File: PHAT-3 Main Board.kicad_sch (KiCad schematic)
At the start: 2 parts, among them U1 BY-68 BMP180, U2 ESP32-S3 Dual-core SX1262

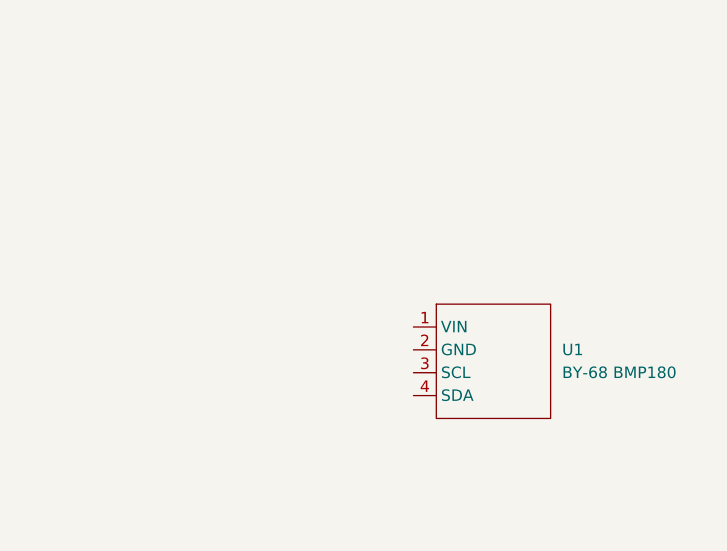
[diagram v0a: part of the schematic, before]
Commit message: Added AHT21 I2C IIC
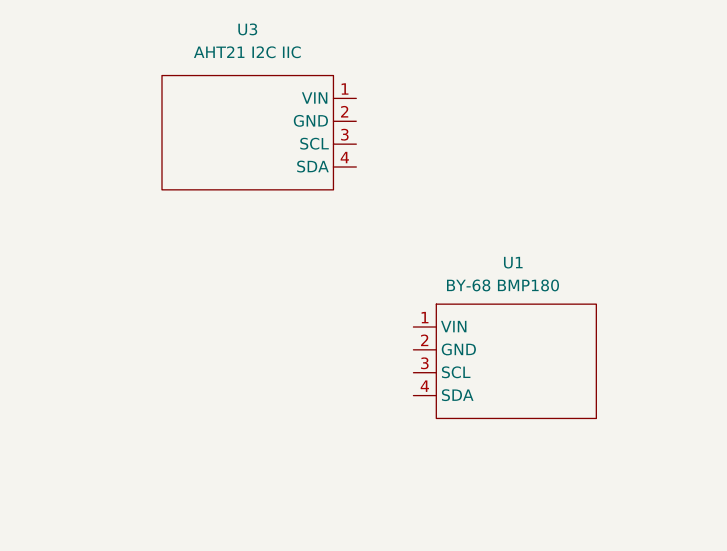
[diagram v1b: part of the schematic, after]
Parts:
- added U3: AHT21 I2C IIC, Actual Footprint Library:AHT21 I2C IIC, symbol Footprint Library:AHT21_I2C_IIC
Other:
- moved on the sheet: U1
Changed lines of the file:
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@@
 	(paper "A4")
+	(symbol
+		(lib_id "Footprint Library:AHT21_I2C_IIC")
+		(at 151.13 66.04 0)
+		(unit 1)
+		(exclude_from_sim no)
+		(in_bom yes)
+		(on_board yes)
+		(dnp no)
+		(fields_autoplaced yes)
+		(property "Reference" "U3"
+			(at 139.065 50.8 0)
+			(effects
+				(font
+					(size 1.27 1.27)
+				)
+			)
+		)
+		(property "Value" "AHT21 I2C IIC"
+			(at 139.065 53.34 0)
+			(effects
+				(font
+					(size 1.27 1.27)
+				)
+			)
+		)
+		(property "Footprint" "Actual Footprint Library:AHT21 I2C IIC"
+			(at 150.368 74.168 0)
+			(effects
+				(font
+					(size 1.27 1.27)
+				)
+				(hide yes)
+			)
+		)
+		(property "Datasheet" ""
+			(at 151.13 66.04 0)
+			(effects
+				(font
+					(size 1.27 1.27)
+				)
+				(hide yes)
+			)
+		)
+		(property "Description" ""
+			(at 151.13 66.04 0)
+			(effects
+				(font
+					(size 1.27 1.27)
+				)
+				(hide yes)
+			)
+		)
+		(pin "1"
+		)
+		(pin "2"
+		)
+		(pin "3"
+		)
+		(pin "4"
+		)
+		(instances
+			(project ""
+				(path "/da389c8a-9ca2-41c4-a7eb-3ce46ba4333b"
+					(reference "U3")
+					(unit 1)
+				)
+			)
+		)
+	)
 	(symbol
 		(lib_id "Footprint Library:ESP32-S3_Dual-core_SX1262")
@@
 		(on_board yes)
 		(dnp no)
-		(fields_autoplaced yes)
 		(property "Reference" "U1"
-			(at 173.99 86.3599 0)
+			(at 167.386 76.708 0)
 			(effects
 				(font
@@
 		)
 		(property "Value" "BY-68 BMP180"
-			(at 173.99 88.8999 0)
-			(effects
-				(font
+			(at 161.036 79.248 0)
+			(effects
+				(font

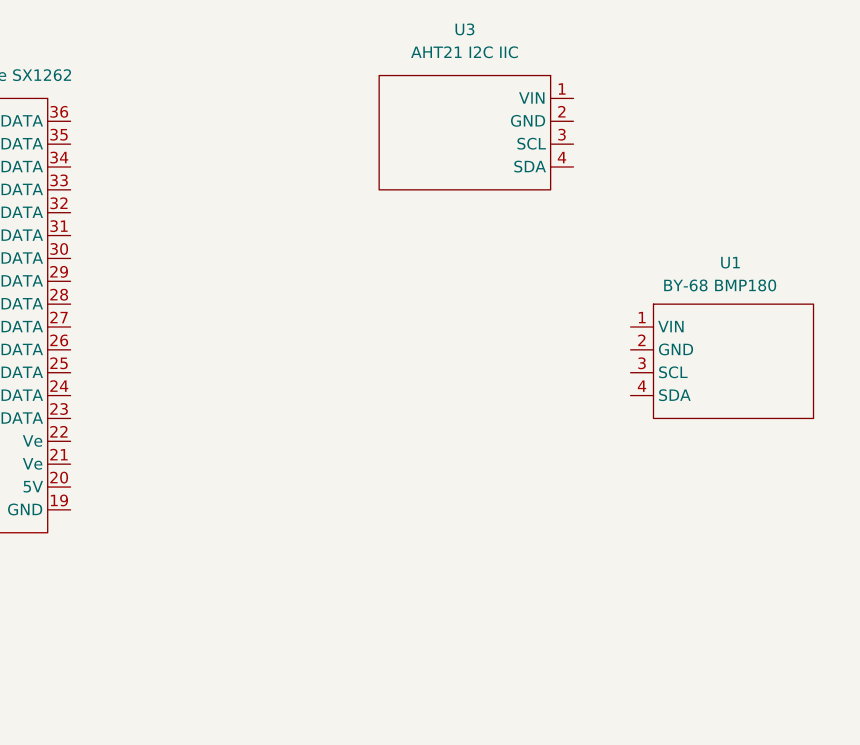
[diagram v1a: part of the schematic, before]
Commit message: Added Buck Converter and Rest of Sensors
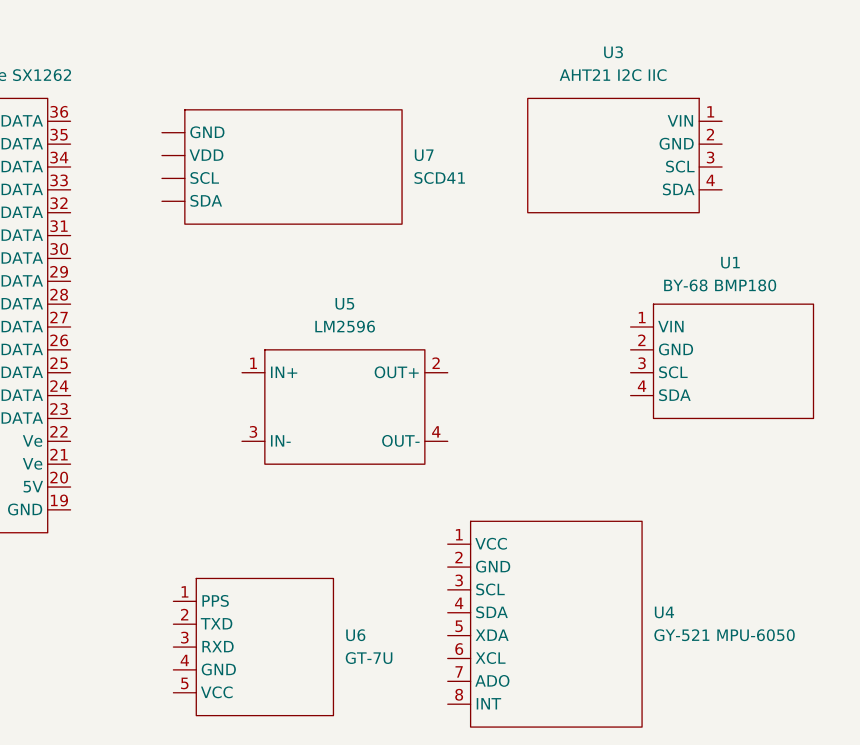
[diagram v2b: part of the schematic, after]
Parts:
- added U4: GY-521 MPU-6050, Actual Footprint Library:GY-521 MPU-6050, symbol Footprint Library:GY-521_MPU-6050
- added U5: LM2596, Actual Footprint Library:LM2596, symbol Footprint Library:LM2596
- added U6: GT-7U, Actual Footprint Library:GT-U7, symbol Footprint Library:GT-7U
- added U7: SCD41, Actual Footprint Library:SCD41, symbol Footprint Library:SCD41
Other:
- moved on the sheet: U3

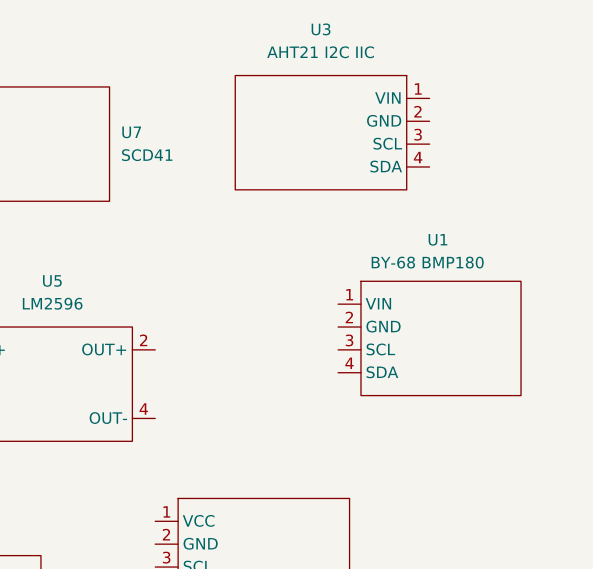
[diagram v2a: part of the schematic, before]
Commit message: Updated GY-BMP180 to BME280
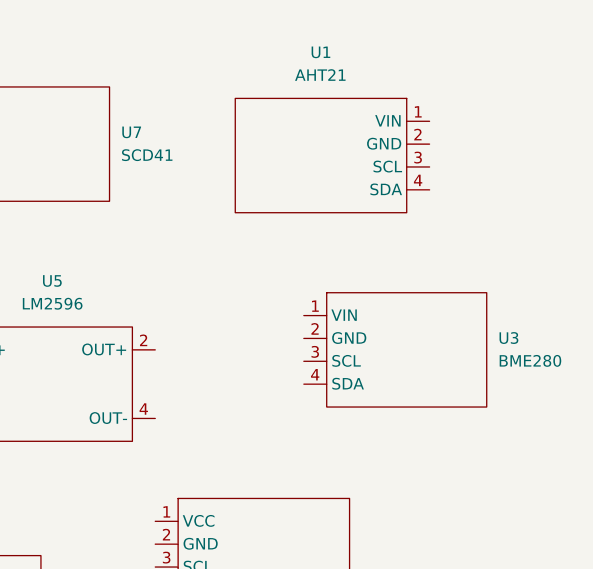
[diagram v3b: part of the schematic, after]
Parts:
- removed U1: BY-68 BMP180, Actual Footprint Library:BY-68 BMP180, symbol Footprint Library:GY-68_BMP180
- removed U3: AHT21 I2C IIC, Actual Footprint Library:AHT21 I2C IIC, symbol Footprint Library:AHT21_I2C_IIC
- added U1: AHT21, Actual Footprint Library:AHT21, symbol Footprint Library:AHT21
- added U3: BME280, Actual Footprint Library:BME280, symbol Footprint Library:BME280
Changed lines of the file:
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@@
-	)
-	(symbol
-		(lib_id "Footprint Library:AHT21_I2C_IIC")
-		(at 167.64 68.58 0)
-		(unit 1)
-		(exclude_from_sim no)
-		(in_bom yes)
-		(on_board yes)
-		(dnp no)
-		(fields_autoplaced yes)
-		(property "Reference" "U3"
-			(at 155.575 53.34 0)
-			(effects
-				(font
-					(size 1.27 1.27)
-				)
-			)
-		)
-		(property "Value" "AHT21 I2C IIC"
-			(at 155.575 55.88 0)
-			(effects
-				(font
-					(size 1.27 1.27)
-				)
-			)
-		)
-		(property "Footprint" "Actual Footprint Library:AHT21 I2C IIC"
-			(at 166.878 76.708 0)
-			(effects
-				(font
-					(size 1.27 1.27)
-				)
-				(hide yes)
-			)
-		)
-		(property "Datasheet" ""
-			(at 167.64 68.58 0)
-			(effects
-				(font
-					(size 1.27 1.27)
-				)
-				(hide yes)
-			)
-		)
-		(property "Description" ""
-			(at 167.64 68.58 0)
-			(effects
-				(font
-					(size 1.27 1.27)
-				)
-				(hide yes)
-			)
-		)
-		(pin "1"
-		)
-		(pin "2"
-		)
-		(pin "3"
-		)
-		(pin "4"
-		)
-		(instances
-			(project ""
-				(path "/da389c8a-9ca2-41c4-a7eb-3ce46ba4333b"
-					(reference "U3")
-					(unit 1)
-				)
-			)
-		)
 	)
 	(symbol
@@
 	)
 	(symbol
+		(lib_id "Footprint Library:AHT21")
+		(at 167.64 71.12 0)
+		(unit 1)
+		(exclude_from_sim no)
+		(in_bom yes)
+		(on_board yes)
+		(dnp no)
+		(fields_autoplaced yes)
+		(property "Reference" "U1"
+			(at 155.575 55.88 0)
+			(effects
+				(font
+					(size 1.27 1.27)
+				)
+			)
+		)
+		(property "Value" "AHT21"
+			(at 155.575 58.42 0)
+			(effects
+				(font
+					(size 1.27 1.27)
+				)
+			)
+		)
+		(property "Footprint" "Actual Footprint Library:AHT21"
+			(at 166.878 79.248 0)
+			(effects
+				(font
+					(size 1.27 1.27)
+				)
+				(hide yes)
+			)
+		)
+		(property "Datasheet" ""
+			(at 167.64 71.12 0)
+			(effects
+				(font
+					(size 1.27 1.27)
+				)
+				(hide yes)
+			)
+		)
+		(property "Description" ""
+			(at 167.64 71.12 0)
+			(effects
+				(font
+					(size 1.27 1.27)
+				)
+				(hide yes)
+			)
+		)
+		(pin "4"
+		)
+		(pin "2"
+		)
+		(pin "1"
+		)
+		(pin "3"
+		)
+		(instances
+			(project ""
+				(path "/da389c8a-9ca2-41c4-a7eb-3ce46ba4333b"
+					(reference "U1")
+					(unit 1)
+				)
+			)
+		)
+	)
+	(symbol
 		(lib_id "Footprint Library:ESP32-S3_Dual-core_SX1262")
 		(at 71.12 104.14 0)
@@
 	)
 	(symbol
-		(lib_id "Footprint Library:GY-68_BMP180")
-		(at 157.48 91.44 0)
+		(lib_id "Footprint Library:BME280")
+		(at 153.67 92.71 0)
 		(unit 1)
 		(exclude_from_sim no)
@@
 		(on_board yes)
 		(dnp no)
-		(property "Reference" "U1"
-			(at 167.386 76.708 0)
+		(fields_autoplaced yes)
+		(property "Reference" "U3"
+			(at 175.26 87.6299 0)
 			(effects
 				(font
@@
 			)
 		)
-		(property "Value" "BY-68 BMP180"
-			(at 161.036 79.248 0)
+		(property "Value" "BME280"
+			(at 175.26 90.1699 0)
 			(effects
 				(font
@@
 			)
 		)
-		(property "Footprint" "Actual Footprint Library:BY-68 BMP180"
-			(at 159.004 100.076 0)
+		(property "Footprint" "Actual Footprint Library:BME280"
+			(at 155.194 101.346 0)
 			(effects
 				(font
@@
 		)
 		(property "Datasheet" ""
-			(at 157.48 91.44 0)
+			(at 153.67 92.71 0)
 			(effects
 				(font
@@
 		)
 		(property "Description" ""
-			(at 157.48 91.44 0)
-			(effects
-				(font
-					(size 1.27 1.27)
-				)
-				(hide yes)
-			)
+			(at 153.67 92.71 0)
+			(effects
+				(font
+					(size 1.27 1.27)
+				)
+				(hide yes)
+			)
+		)
+		(pin "2"
 		)
 		(pin "1"
@@
 		)
 		(pin "4"
-		)
-		(pin "2"
 		)
 		(instances
 			(project ""
 				(path "/da389c8a-9ca2-41c4-a7eb-3ce46ba4333b"
-					(reference "U1")
+					(reference "U3")
 					(unit 1)
 				)

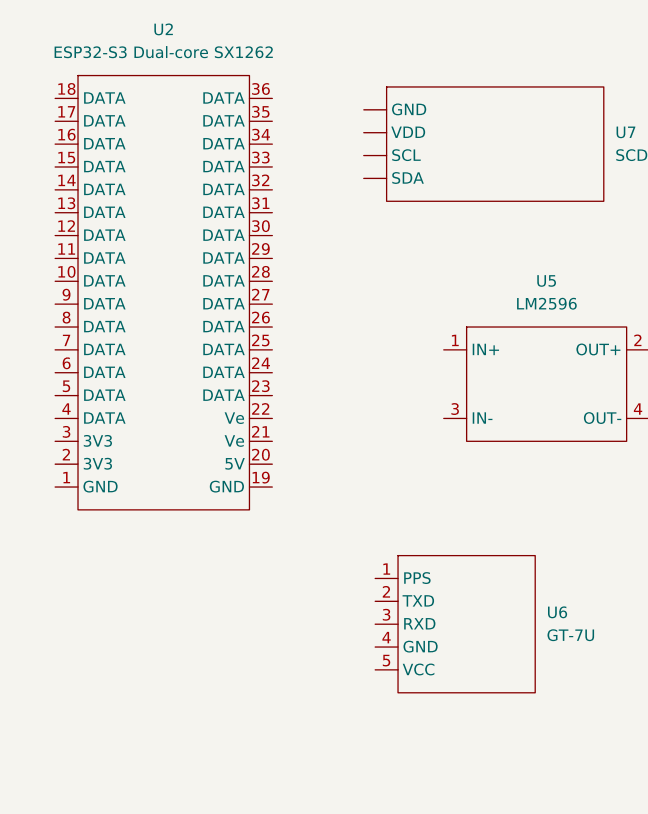
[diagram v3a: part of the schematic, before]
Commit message: Updated Footprint Sizes and Started Adding uCAM-III
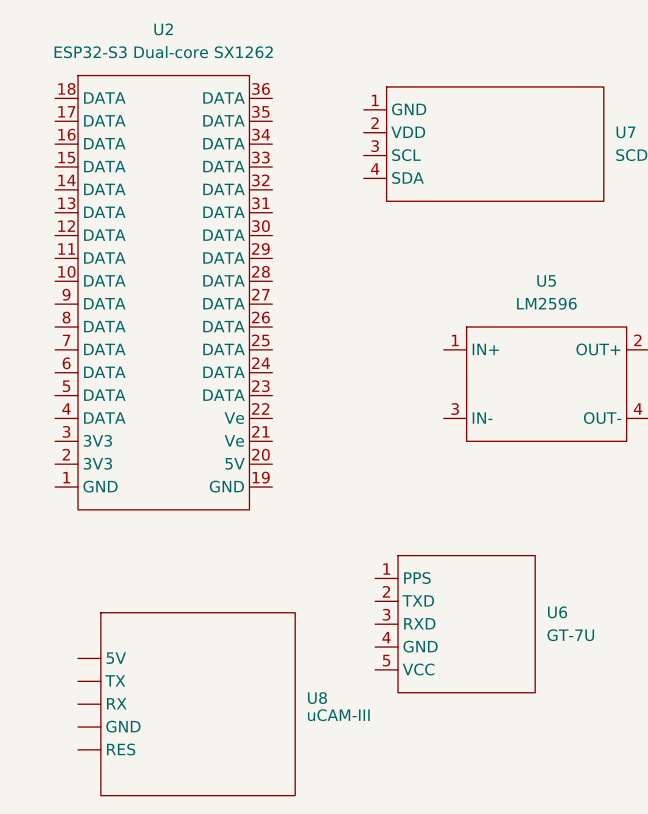
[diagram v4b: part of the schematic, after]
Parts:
- added U8: uCAM-III, symbol Footprint Library:uCAM-III
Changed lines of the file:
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@@
+	)
+	(symbol
+		(lib_id "Footprint Library:uCAM-III")
+		(at 76.2 133.35 0)
+		(unit 1)
+		(exclude_from_sim no)
+		(in_bom yes)
+		(on_board yes)
+		(dnp no)
+		(fields_autoplaced yes)
+		(property "Reference" "U8"
+			(at 99.06 127.6349 0)
+			(effects
+				(font
+					(size 1.27 1.27)
+				)
+				(justify left)
+			)
+		)
+		(property "Value" "uCAM-III"
+			(at 99.06 129.54 0)
+			(effects
+				(font
+					(size 1.27 1.27)
+				)
+				(justify left)
+			)
+		)
+		(property "Footprint" ""
+			(at 76.2 133.35 0)
+			(effects
+				(font
+					(size 1.27 1.27)
+				)
+				(hide yes)
+			)
+		)
+		(property "Datasheet" ""
+			(at 76.2 133.35 0)
+			(effects
+				(font
+					(size 1.27 1.27)
+				)
+				(hide yes)
+			)
+		)
+		(property "Description" ""
+			(at 76.2 133.35 0)
+			(effects
+				(font
+					(size 1.27 1.27)
+				)
+				(hide yes)
+			)
+		)
+		(pin ""
+		)
+		(pin ""
+		)
+		(pin ""
+		)
+		(pin ""
+		)
+		(pin ""
+		)
+		(instances
+			(project ""
+				(path "/da389c8a-9ca2-41c4-a7eb-3ce46ba4333b"
+					(reference "U8")
+					(unit 1)
+				)
+			)
+		)
 	)
 	(symbol
@@
 			)
 		)
-		(pin ""
-		)
-		(pin ""
-		)
-		(pin ""
-		)
-		(pin ""
-		)
-		(instances
+		(pin "1"
+		)
+		(pin "2"
+		)
+		(pin "3"
+		)
+		(pin "4"
+		)
+		(instances

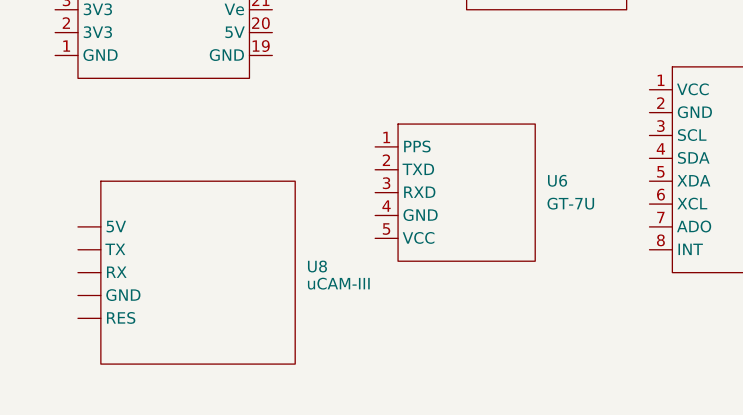
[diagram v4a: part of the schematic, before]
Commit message: Finished Adding uCAM-III
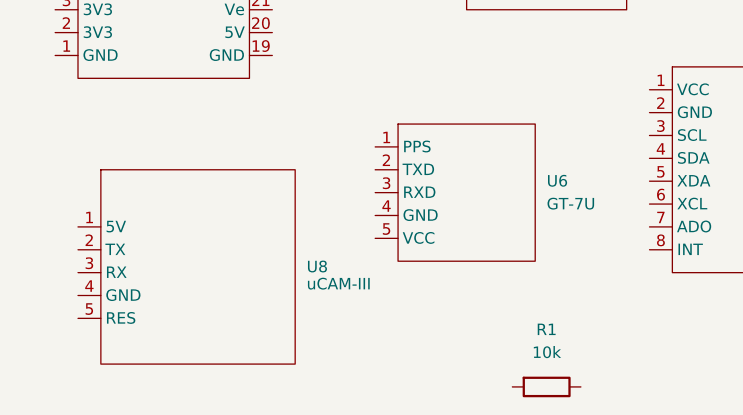
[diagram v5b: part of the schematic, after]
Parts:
- added R1: 10k, Resistor_THT:R_Axial_DIN0207_L6.3mm_D2.5mm_P10.16mm_Horizontal, symbol Device:R
- U8: footprint (none) -> Actual Footprint Library:uCAM-III
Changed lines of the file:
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@@
 			)
 		)
-		(property "Footprint" ""
+		(property "Footprint" "Actual Footprint Library:uCAM-III"
 			(at 76.2 133.35 0)
 			(effects
@@
 			)
 		)
-		(pin ""
-		)
-		(pin ""
-		)
-		(pin ""
-		)
-		(pin ""
-		)
-		(pin ""
+		(pin "5"
+		)
+		(pin "3"
+		)
+		(pin "1"
+		)
+		(pin "4"
+		)
+		(pin "2"
 		)
 		(instances
@@
 					(unit 1)
 				)
+			)
+		)
+	)
+	(symbol
+		(lib_id "Device:R")
+		(at 125.73 140.97 270)
+		(unit 1)
+		(exclude_from_sim no)
+		(in_bom yes)
+		(on_board yes)
+		(dnp no)
+		(fields_autoplaced yes)
+		(property "Reference" "R1"
+			(at 125.73 134.62 90)
+			(effects
+				(font
+					(size 1.27 1.27)
+				)
+			)
+		)
+		(property "Value" "10k"
+			(at 125.73 137.16 90)
+			(effects
+				(font
+					(size 1.27 1.27)
+				)
+			)
+		)
+		(property "Footprint" "Resistor_THT:R_Axial_DIN0207_L6.3mm_D2.5mm_P10.16mm_Horizontal"
+			(at 125.73 139.192 90)
+			(effects
+				(font
+					(size 1.27 1.27)
+				)
+				(hide yes)
+			)
+		)
+		(property "Datasheet" "~"
+			(at 125.73 140.97 0)
+			(effects
+				(font
+					(size 1.27 1.27)
+				)
+				(hide yes)
+			)
+		)
+		(property "Description" "Resistor"
+			(at 125.73 140.97 0)
+			(effects
+				(font
+					(size 1.27 1.27)
+				)
+				(hide yes)
+			)
+		)
+		(pin "2"
+		)
+		(pin "1"
+		)
+		(instances
+			(project ""
+				(path "/da389c8a-9ca2-41c4-a7eb-3ce46ba4333b"
+					(reference "R1")
+					(unit 1)
+				)
